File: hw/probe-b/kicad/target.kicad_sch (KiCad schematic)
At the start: 51 parts, among them J2 MIPI20, Q1 2N7002, U11 TPD4E02B04DQA, U12 TPD4E02B04DQA, U13 TPD4E02B04DQA, U14 SN74AVC8T245PW, U15 SN74AVC4T245PW, U16 AP2161W, U17 INA219AxD, U18 ADS1115IDGS

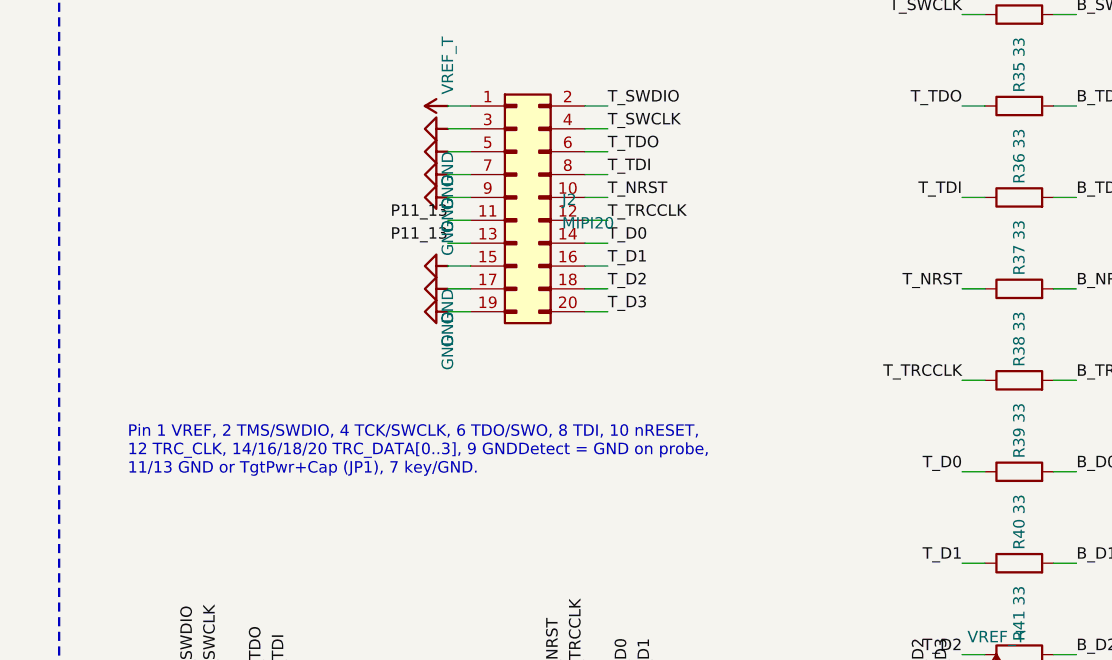
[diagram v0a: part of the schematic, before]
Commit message: MIPI20: требования к шлейфу, вывод 7 — ключ (удалён на вилках)
Co-Authored-By: Claude Opus 5.5 <noreply@anthropic.com>
Claude-Session: https://claude.ai/code/session_01C2rXcGumdBomkHLEESi7ny
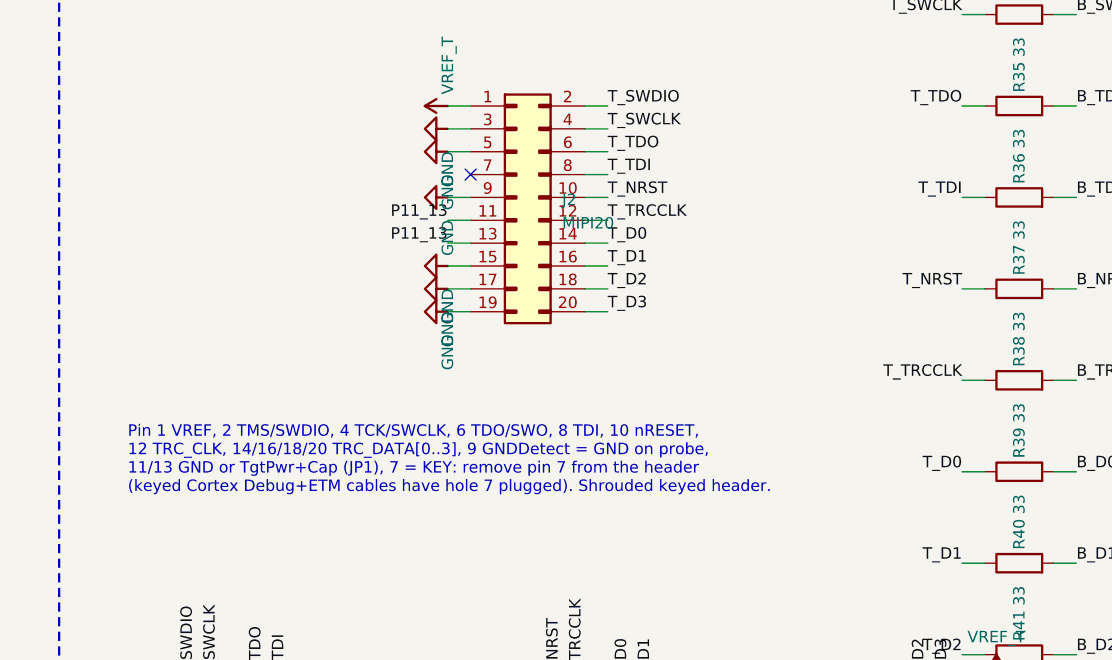
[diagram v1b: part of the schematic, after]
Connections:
- net GND: no longer J2.7 (Pin_7)
- no-connect marks 2 -> 3
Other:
- note added: "Pin 1 VREF, 2 TMS/SWDIO, 4 TCK/SWCLK, 6 TDO/SWO, 8 TDI, 10 nRESET, 12 TRC_CLK, 14/16/18/20 TRC_DATA[0..3], 9 GNDDetect = GND on probe, 11/13 GND or TgtPwr+Cap (JP1), 7 = KEY: remove pin 7 from the header (keyed Cortex Debug+ETM cables have hole 7 plugged). Shrouded keyed header."
- note removed: "Pin 1 VREF, 2 TMS/SWDIO, 4 TCK/SWCLK, 6 TDO/SWO, 8 TDI, 10 nRESET, 12 TRC_CLK, 14/16/18/20 TRC_DATA[0..3], 9 GNDDetect = GND on probe, 11/13 GND or TgtPwr+Cap (JP1), 7 key/GND."
